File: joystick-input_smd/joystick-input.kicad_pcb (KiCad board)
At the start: 2 copper layers, 53.3 x 29.5 mm, 18 parts, among them J1 Conn_01x18, J2 Conn_02x14_Odd_Even

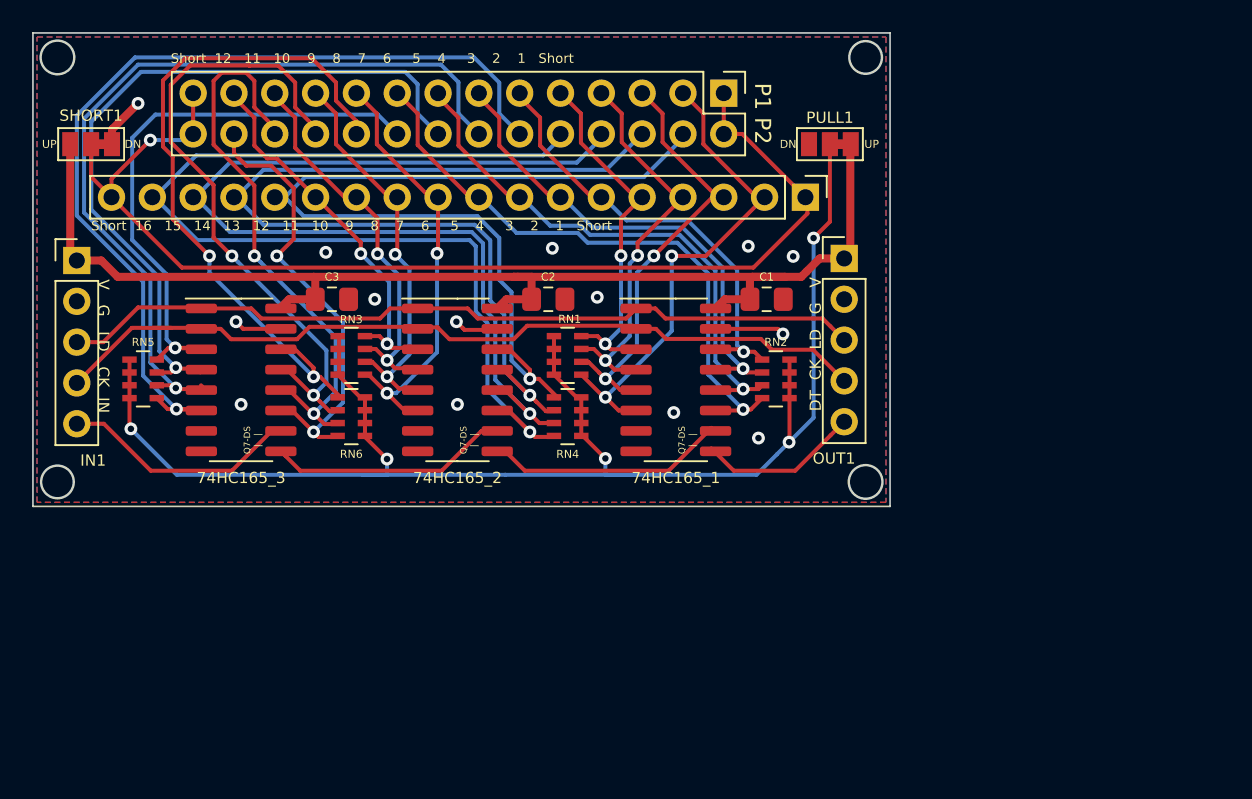
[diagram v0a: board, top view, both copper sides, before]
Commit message: 오드로이드n2용 io 확장보드 추가
Signed-off-by: Ju, Gyeong-min <jcmh74@gmail.com>
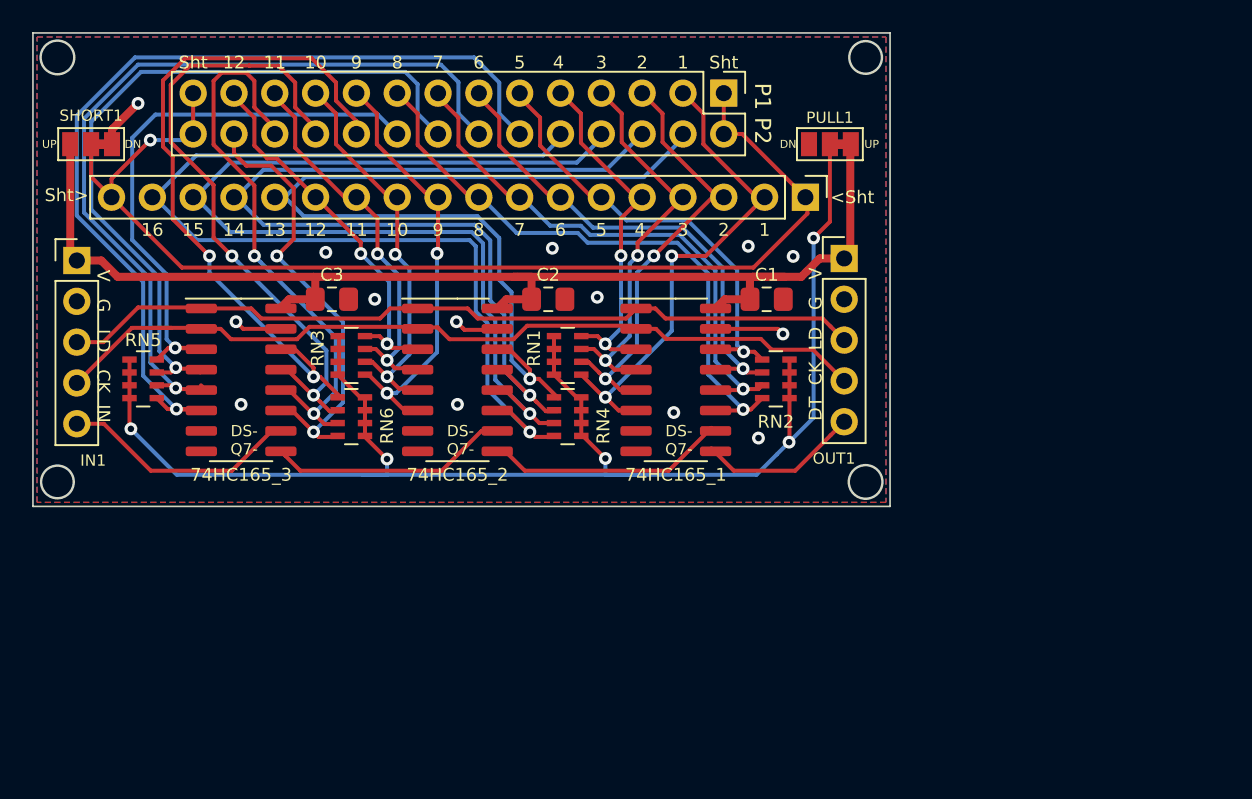
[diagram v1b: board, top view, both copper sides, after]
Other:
- board text added: "1"
- board text added: "10"
- board text added: "11"
- board text added: "12"
- board text added: "13"
- board text added: "14"
- board text added: "15"
- board text added: "16"
- board text added: "2"
- board text added: "3"
- board text added: "4"
- board text added: "5"
- board text added: "6"
- board text added: "7"
- board text added: "8"
- board text added: "9"
- board text added: "<Sht"
- board text added: "DS- Q7-"
- board text added: "Sht"
- board text added: "Sht>"
- board text removed: "Q7-DS | |"
- board text removed: "Short 12 11 10 9 8 7 6 5 4 3 2 1 Short"
- board text removed: "Short 16 15 14 13 12 11 10 9 8 7 6 5 4 3 2 1 Short"

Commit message: joystick-input_2p 스크린샷
Signed-off-by: Ju, Gyeong-min <jcmh74@gmail.com>
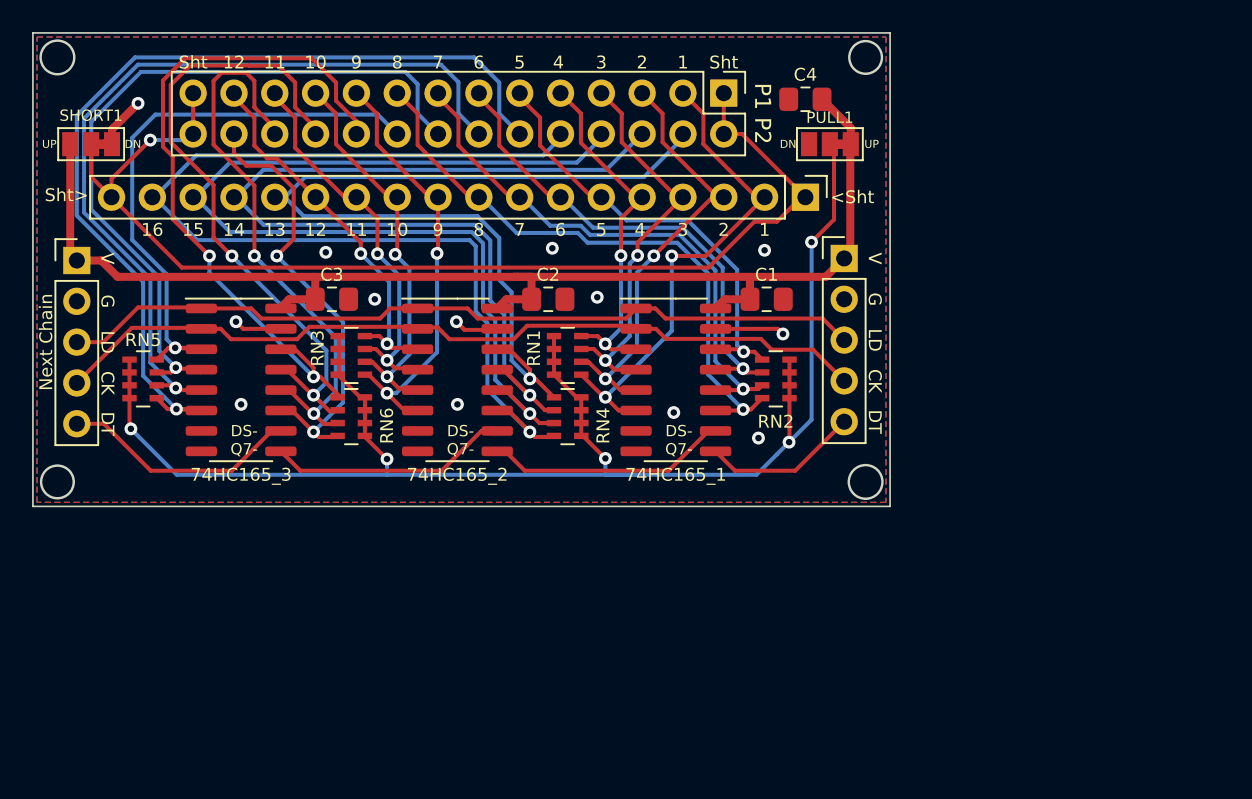
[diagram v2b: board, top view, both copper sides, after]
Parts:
- added C4: C, Capacitor_SMD:C_0805_2012Metric_Pad1.18x1.45mm_HandSolder, F.Cu at (159.9, 71.9)
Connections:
- 74HC165_1 pad 7: (no net) -> unconnected-(74HC165_1-Pad7)
- 74HC165_2 pad 7: (no net) -> unconnected-(74HC165_2-Pad7)
- 74HC165_3 pad 7: (no net) -> unconnected-(74HC165_3-Pad7)
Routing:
- net /C_SHORT: track 71.4 -> 69.9 mm
- net VCC: track 78.1 -> 79.4 mm
- net /PULL: track 95.8 -> 94.5 mm
- net /CLK: track 53.2 -> 52.0 mm
- net GND: vias 14 -> 13
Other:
- net class Default removed
- net class Power removed
- board text added: "CK"
- board text added: "DT"
- board text added: "G"
- board text added: "LD"
- board text added: "Next Chain"
- board text added: "V"
- board text removed: "DT CK LD G V"
- board text removed: "V G LD CK IN"

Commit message: joystick_input 레이아웃 변경
Signed-off-by: Ju, Gyeong-min <jcmh74@gmail.com>
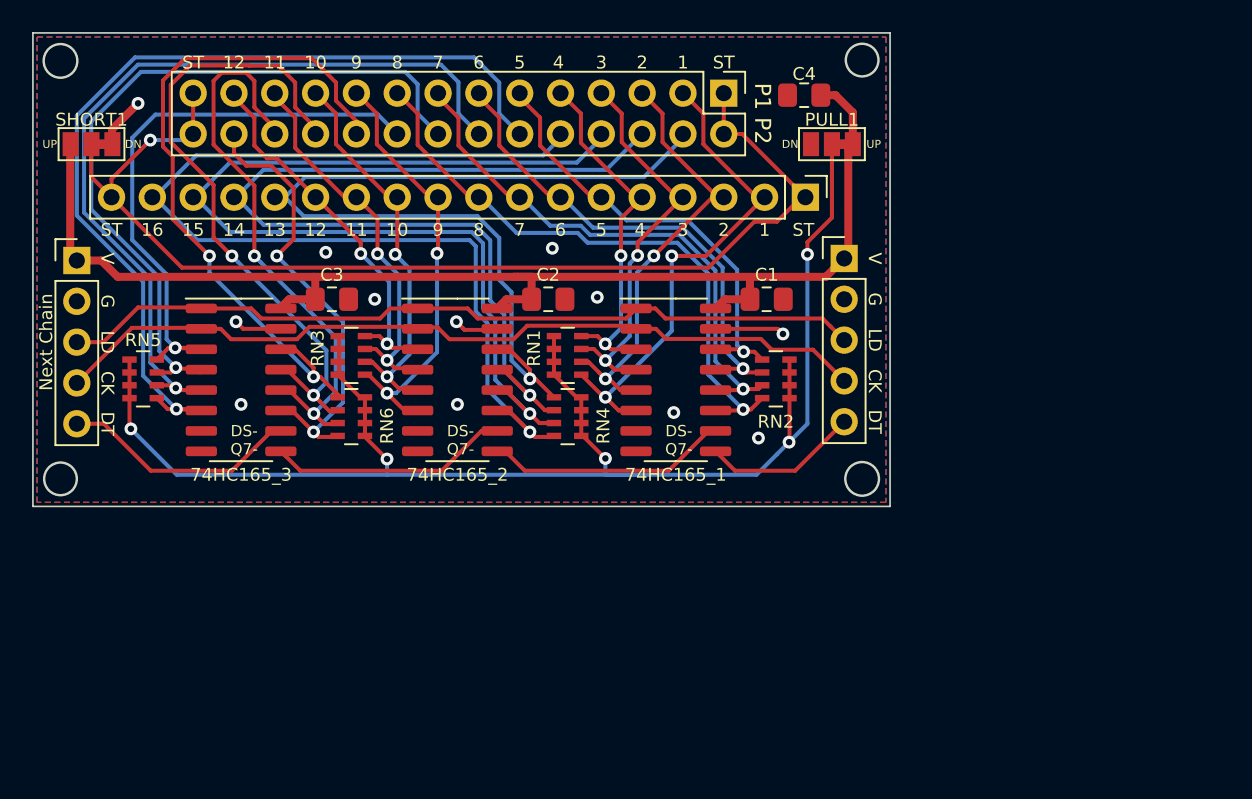
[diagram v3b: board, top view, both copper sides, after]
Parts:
- moved C4 0.27 mm to (159.8, 71.6)
- moved PULL1 0.13 mm to (161.5, 74.7)
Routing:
- net VCC: track 79.4 -> 80.3 mm
- net GND: vias 13 -> 12
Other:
- outline, holes or cut-outs redrawn
- board text added: "ST"
- board text removed: "<Sht"
- board text removed: "Sht"
- board text removed: "Sht>"

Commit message: 도면 시트 설명 추가
Signed-off-by: Ju, Gyeong-min <jcmh74@gmail.com>
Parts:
- moved 74HC165_1 26.1 mm to (172.3, 105.5)
- moved 74HC165_2 26.1 mm to (158.7, 105.5)
- moved 74HC165_3 26.1 mm to (145.2, 105.5)
- moved J1 26.1 mm to (180.3, 94.1)
- moved RN1 26.1 mm to (165.5, 104.0)
- moved RN3 26.1 mm to (152.1, 104.0)
- moved C1 26.1 mm to (177.9, 100.5)
- moved C2 26.1 mm to (164.3, 100.5)
- moved C3 26.1 mm to (150.9, 100.5)
- moved C4 26.1 mm to (180.3, 87.8)
- moved IN1 26.1 mm to (135.0, 98.1)
- moved J2 26.1 mm to (175.3, 87.7)
- moved PULL1 26.1 mm to (182.0, 90.8)
- moved RN2 26.1 mm to (178.5, 105.4)
- moved RN4 26.1 mm to (165.5, 107.8)
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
